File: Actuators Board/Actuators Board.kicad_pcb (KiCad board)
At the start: 2 copper layers, 89 parts, among them IC1 BD62120AEFJ-E2, J10 Conn_01x02_Male, J3 USB_C_Receptacle_USB2.0, J4 Conn_01x03_Male, J5 Conn_01x06_Male, J9 Conn_01x02_Male, Q1 MMDT2222A, Q2 SI2366DS, U1 ESP32-PICO-D4, U2 TPS54233D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

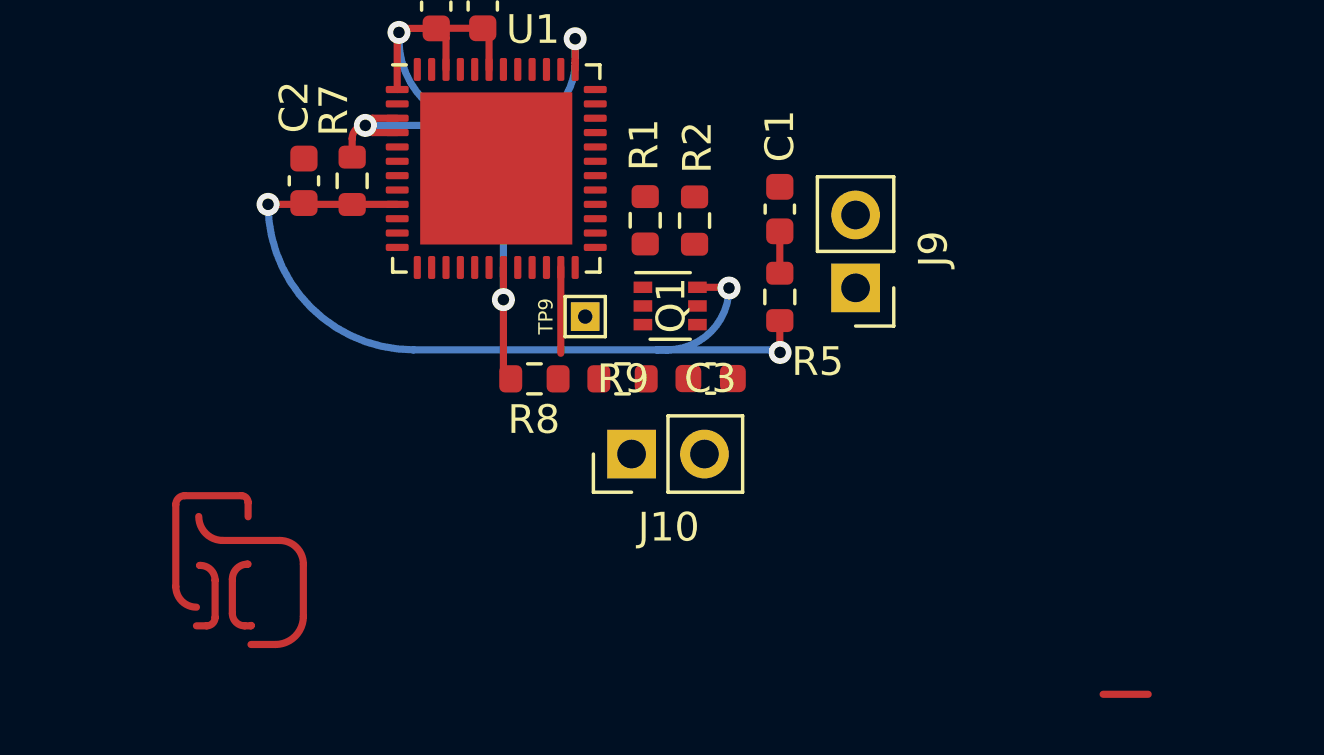
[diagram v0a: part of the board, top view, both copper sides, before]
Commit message: Fixed github's merge attempt
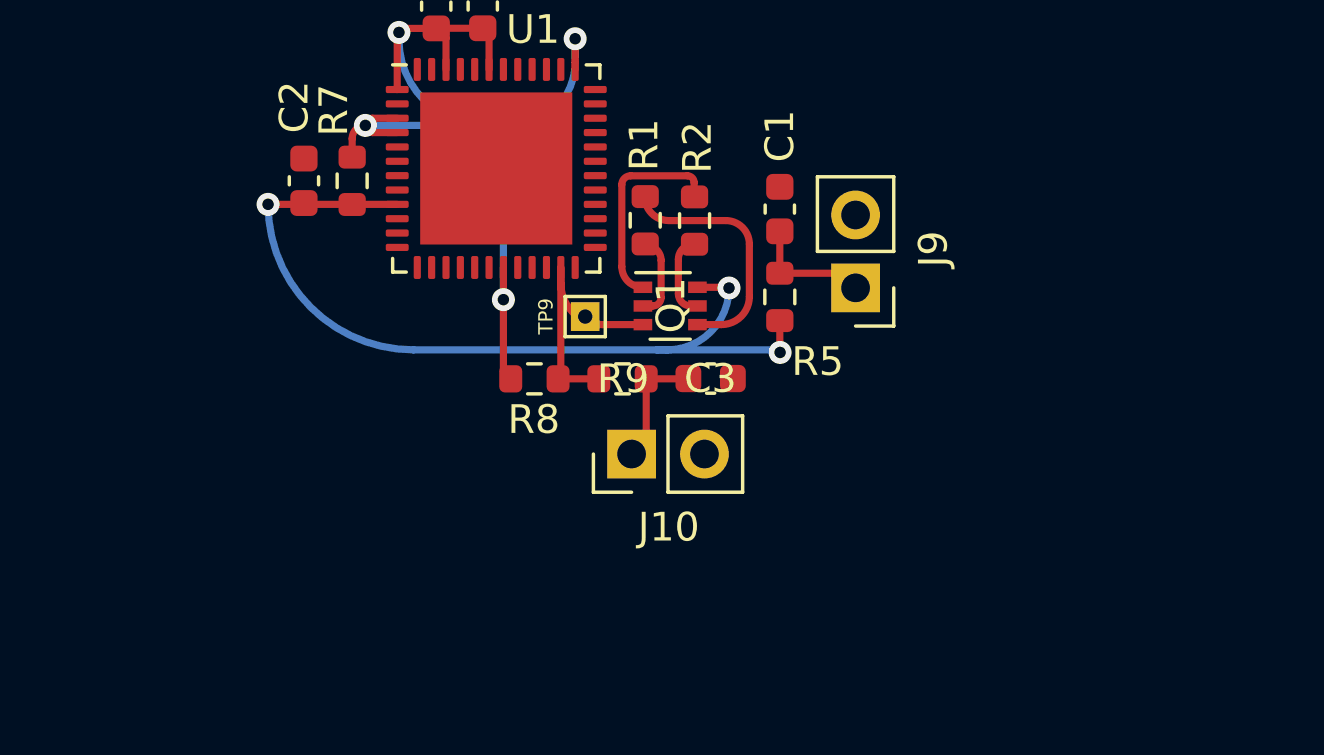
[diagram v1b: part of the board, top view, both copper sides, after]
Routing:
- net /BOOT: track 4.56 -> 9.52 mm
- net Net-(C3-Pad1): track 0.00 -> 4.37 mm
- net Net-(C1-Pad1): track 1.48 -> 4.39 mm
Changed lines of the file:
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@@
     (fp_line (start -2.125 -1.3) (end 2.125 -1.3) (layer "F.Fab") (width 0.127))
     (fp_line (start 2.125 1.3) (end -2.125 1.3) (layer "F.Fab") (width 0.127))
+    (fp_line (start 2.125 -1.3) (end 2.125 1.3) (layer "F.Fab") (width 0.127))
     (fp_line (start -2.125 1.3) (end -2.125 -1.3) (layer "F.Fab") (width 0.127))
-    (fp_line (start 2.125 -1.3) (end 2.125 1.3) (layer "F.Fab") (width 0.127))
     (pad "A" smd rect locked (at 2.01 0 90) (size 1.5 1.52) (layers "F.Cu" "F.Paste" "F.Mask")
       (net 2 "GND") (pintype "passive"))
@@
     )
   )
+  (segment (start 218.79 145.31) (end 220.92 145.31) (width 0.25) (layer "F.Cu") (net 1))
   (segment (start 218.805 145.295) (end 218.79 145.31) (width 0.25) (layer "F.Cu") (net 1))
   (segment (start 218.79 145.31) (end 218.79 143.85) (width 0.25) (layer "F.Cu") (net 1))
+  (arc (start 220.92 145.31) (mid 221.280624 145.459376) (end 221.43 145.82) (width 0.25) (layer "F.Cu") (net 1))
   (segment (start 213.84 45.2) (end 215.905 45.2) (width 0.25) (layer "F.Cu") (net 2))
   (segment (start 76.095002 104.979998) (end 76.095002 102.404998) (width 0.7) (layer "F.Cu") (net 2))
@@
   (arc (start 218.8 148.07) (mid 218.77364 148.00636) (end 218.71 147.98) (width 0.25) (layer "B.Cu") (net 3))
   (arc (start 206.03 147.98) (mid 202.444969 146.495031) (end 200.96 142.91) (width 0.25) (layer "B.Cu") (net 3))
+  (segment (start 214.135 151.1) (end 214.135 148.99) (width 0.25) (layer "F.Cu") (net 4))
+  (segment (start 214.135 148.99) (end 215.595 148.99) (width 0.25) (layer "F.Cu") (net 4))
+  (arc (start 213.625 151.61) (mid 213.985624 151.460624) (end 214.135 151.1) (width 0.25) (layer "F.Cu") (net 4))
+  (arc (start 215.595 148.99) (mid 215.602071 148.987071) (end 215.605 148.98) (width 0.25) (layer "F.Cu") (net 4))
   (segment (start 202.955 39.8525) (end 213.0625 39.8525) (width 0.25) (layer "F.Cu") (net 5))
   (segment (start 208.44 136.775) (end 206.825 136.775) (width 0.25) (layer "F.Cu") (net 5))
@@
   (segment (start 71.243002 95.809998) (end 68.130002 95.809998) (width 0.7) (layer "F.Cu") (net 24))
   (arc (start 68.130002 95.809998) (mid 68.119395 95.805605) (end 68.115002 95.794998) (width 0.7) (layer "F.Cu") (net 24))
-  (segment (start 197.745724 156.225724) (end 197.745724 153.367981) (width 0.25) (layer "F.Cu") (net 27))
-  (segment (start 198.052981 153.060724) (end 200.031825 153.060724) (width 0.25) (layer "F.Cu") (net 27))
-  (segment (start 200.265244 153.795244) (end 200.265244 153.294143) (width 0.25) (layer "F.Cu") (net 27))
-  (arc (start 198.465244 156.945244) (mid 197.956467 156.734501) (end 197.745724 156.225724) (width 0.25) (layer "F.Cu") (net 27))
-  (arc (start 200.031825 153.060724) (mid 200.196877 153.129091) (end 200.265244 153.294143) (width 0.25) (layer "F.Cu") (net 27))
-  (arc (start 197.745724 153.367981) (mid 197.835717 153.150717) (end 198.052981 153.060724) (width 0.25) (layer "F.Cu") (net 27))
-  (segment (start 231.625 159.98) (end 230.055 159.98) (width 0.25) (layer "F.Cu") (net 28))
-  (segment (start 211.16 145.11) (end 211.16 148.1) (width 0.25) (layer "F.Cu") (net 28))
-  (segment (start 200.240504 155.445244) (end 200.265244 155.445244) (width 0.25) (layer "F.Cu") (net 29))
-  (segment (start 199.715733 157.165733) (end 199.715733 155.970015) (width 0.25) (layer "F.Cu") (net 29))
-  (segment (start 200.365244 157.595244) (end 200.145244 157.595244) (width 0.25) (layer "F.Cu") (net 29))
-  (arc (start 200.145244 157.595244) (mid 199.841534 157.469443) (end 199.715733 157.165733) (width 0.25) (layer "F.Cu") (net 29))
-  (arc (start 200.380244 157.580244) (mid 200.369637 157.584637) (end 200.365244 157.595244) (width 0.25) (layer "F.Cu") (net 29))
-  (arc (start 199.715733 155.970015) (mid 199.869435 155.598946) (end 200.240504 155.445244) (width 0.25) (layer "F.Cu") (net 29))
-  (segment (start 199.114755 156.004755) (end 199.114755 157.301222) (width 0.25) (layer "F.Cu") (net 30))
-  (segment (start 198.6 155.49) (end 198.57 155.49) (width 0.25) (layer "F.Cu") (net 30))
-  (segment (start 198.820733 157.595244) (end 198.465244 157.595244) (width 0.25) (layer "F.Cu") (net 30))
-  (arc (start 199.114755 157.301222) (mid 199.028638 157.509127) (end 198.820733 157.595244) (width 0.25) (layer "F.Cu") (net 30))
-  (arc (start 199.114755 156.004755) (mid 198.963987 155.640768) (end 198.6 155.49) (width 0.25) (layer "F.Cu") (net 30))
-  (segment (start 202.189755 155.44035) (end 202.189755 157.270347) (width 0.25) (layer "F.Cu") (net 31))
-  (segment (start 199.380244 154.620244) (end 201.369649 154.620244) (width 0.25) (layer "F.Cu") (net 31))
-  (segment (start 201.214858 158.245244) (end 200.365244 158.245244) (width 0.25) (layer "F.Cu") (net 31))
-  (arc (start 199.380244 154.620244) (mid 198.78981 154.375678) (end 198.545244 153.785244) (width 0.25) (layer "F.Cu") (net 31))
-  (arc (start 202.189755 157.270347) (mid 201.904214 157.959703) (end 201.214858 158.245244) (width 0.25) (layer "F.Cu") (net 31))
-  (arc (start 201.369649 154.620244) (mid 201.949552 154.860447) (end 202.189755 155.44035) (width 0.25) (layer "F.Cu") (net 31))
+  (segment (start 213.28522 145.080477) (end 213.28522 142.222737) (width 0.25) (layer "F.Cu") (net 27))
+  (segment (start 213.592477 141.91548) (end 215.571321 141.91548) (width 0.25) (layer "F.Cu") (net 27))
+  (segment (start 215.80474 142.65) (end 215.80474 142.148899) (width 0.25) (layer "F.Cu") (net 27))
+  (arc (start 214.00474 145.8) (mid 213.495962 145.589256) (end 213.28522 145.080477) (width 0.25) (layer "F.Cu") (net 27))
+  (arc (start 215.571321 141.91548) (mid 215.736373 141.983847) (end 215.80474 142.148899) (width 0.25) (layer "F.Cu") (net 27))
+  (arc (start 213.28522 142.222737) (mid 213.375213 142.005473) (end 213.592477 141.91548) (width 0.25) (layer "F.Cu") (net 27))
+  (segment (start 211.16 145.11) (end 211.16 149.02) (width 0.25) (layer "F.Cu") (net 28))
+  (segment (start 214.02 147.1) (end 212.601712 147.1) (width 0.25) (layer "F.Cu") (net 28))
+  (segment (start 211.16 145.658288) (end 211.16 145.11) (width 0.25) (layer "F.Cu") (net 28))
+  (segment (start 212.485 148.99) (end 211.065 148.99) (width 0.25) (layer "F.Cu") (net 28))
+  (arc (start 212.601712 147.1) (mid 211.582268 146.677732) (end 211.16 145.658288) (width 0.25) (layer "F.Cu") (net 28))
+  (arc (start 211.16 149.02) (mid 211.157071 149.027071) (end 211.15 149.03) (width 0.25) (layer "F.Cu") (net 28))
+  (segment (start 215.78 144.3) (end 215.80474 144.3) (width 0.25) (layer "F.Cu") (net 29))
+  (segment (start 215.255229 146.020489) (end 215.255229 144.824771) (width 0.25) (layer "F.Cu") (net 29))
+  (segment (start 215.90474 146.45) (end 215.68474 146.45) (width 0.25) (layer "F.Cu") (net 29))
+  (arc (start 215.68474 146.45) (mid 215.38103 146.324199) (end 215.255229 146.020489) (width 0.25) (layer "F.Cu") (net 29))
+  (arc (start 215.91974 146.435) (mid 215.909133 146.439393) (end 215.90474 146.45) (width 0.25) (layer "F.Cu") (net 29))
+  (arc (start 215.255229 144.824771) (mid 215.408931 144.453702) (end 215.78 144.3) (width 0.25) (layer "F.Cu") (net 29))
+  (segment (start 214.654251 144.859511) (end 214.654251 146.155978) (width 0.25) (layer "F.Cu") (net 30))
+  (segment (start 214.139496 144.344756) (end 214.109496 144.344756) (width 0.25) (layer "F.Cu") (net 30))
+  (segment (start 214.360229 146.45) (end 214.00474 146.45) (width 0.25) (layer "F.Cu") (net 30))
+  (arc (start 214.654251 146.155978) (mid 214.568134 146.363883) (end 214.360229 146.45) (width 0.25) (layer "F.Cu") (net 30))
+  (arc (start 214.654251 144.859511) (mid 214.503483 144.495524) (end 214.139496 144.344756) (width 0.25) (layer "F.Cu") (net 30))
+  (segment (start 217.729251 144.295106) (end 217.729251 146.125103) (width 0.25) (layer "F.Cu") (net 31))
+  (segment (start 214.91974 143.475) (end 216.909145 143.475) (width 0.25) (layer "F.Cu") (net 31))
+  (segment (start 216.754354 147.1) (end 215.90474 147.1) (width 0.25) (layer "F.Cu") (net 31))
+  (arc (start 214.91974 143.475) (mid 214.329306 143.230434) (end 214.08474 142.64) (width 0.25) (layer "F.Cu") (net 31))
+  (arc (start 217.729251 146.125103) (mid 217.44371 146.814459) (end 216.754354 147.1) (width 0.25) (layer "F.Cu") (net 31))
+  (arc (start 216.909145 143.475) (mid 217.489048 143.715203) (end 217.729251 144.295106) (width 0.25) (layer "F.Cu") (net 31))
   (segment (start 183.545 147.32) (end 181.78 147.32) (width 0.25) (layer "F.Cu") (net 34))
   (segment (start 181.715 146.21) (end 181.715 147.385) (width 0.25) (layer "F.Cu") (net 34))

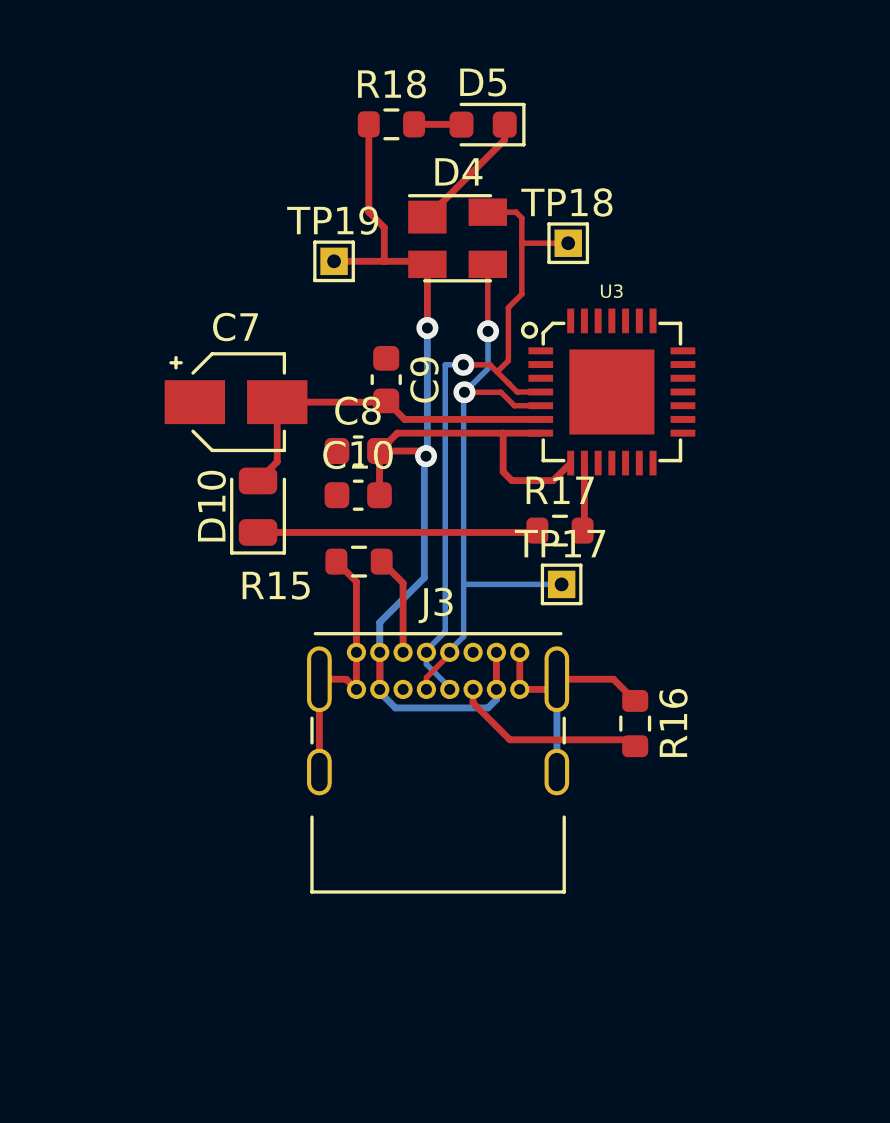
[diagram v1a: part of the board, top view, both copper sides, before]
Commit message: Changed usb layout
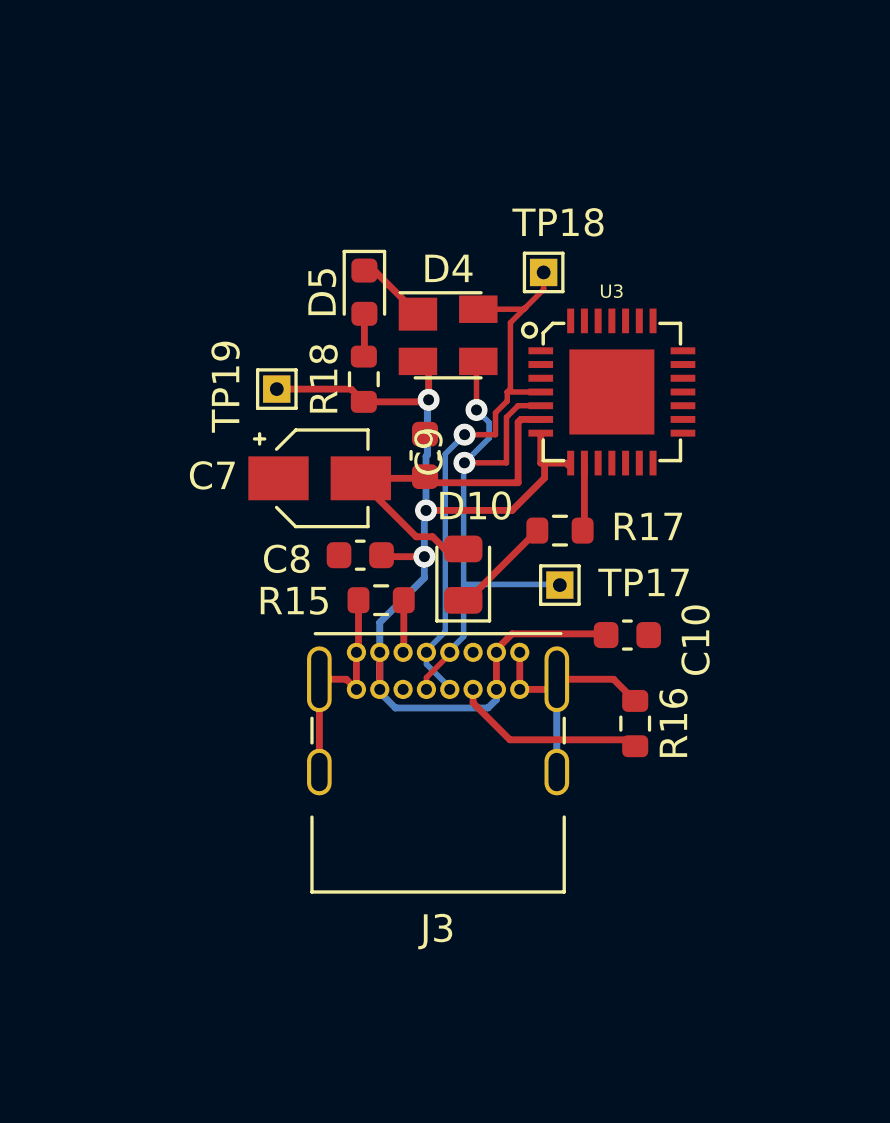
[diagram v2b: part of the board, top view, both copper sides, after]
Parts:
- moved C10 11.0 mm to (216.4, 43.6), turned to 180 degrees
- moved R18 9.34 mm to (206.8, 34.3), turned to 90 degrees
- moved D10 7.87 mm to (210.4, 41.4)
- moved D5 7.48 mm to (206.8, 31.1), turned to -90 degrees
- moved TP19 5.10 mm to (203.6, 34.6)
- moved C7 4.12 mm to (205.2, 37.9)
- moved C8 3.80 mm to (206.7, 40.7)
- moved D4 3.55 mm to (209.9, 32.7)
- moved C9 3.10 mm to (209.0, 37.0)
- moved R15 1.62 mm to (207.4, 42.3)
- moved TP18 1.39 mm to (213.4, 30.4)
- moved TP17 0.07 mm to (213.9, 41.8)
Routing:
- net +3V3: track 51.6 -> 45.2 mm
- net VBUS: track 46.5 -> 40.2 mm, vias 2 -> 3
- net /USB -> UART/Data+: track 25.4 -> 20.9 mm
- net GND: track 35.5 -> 31.9 mm
- net Net-(J3-PadA5): track 3.63 -> 1.91 mm
- net /USB -> UART/Data-: track 23.2 -> 21.6 mm
- net Net-(C7-Pad2): track 13.1 -> 13.8 mm
